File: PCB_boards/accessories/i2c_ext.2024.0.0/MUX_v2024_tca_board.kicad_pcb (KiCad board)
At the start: 2 copper layers, 75 x 50 mm, 18 parts, among them J1 I2C, J2 I2C, J3 I2C, J4 I2C, J5 I2C, J6 I2C, J7 I2C, J8 I2C, J9 I2C

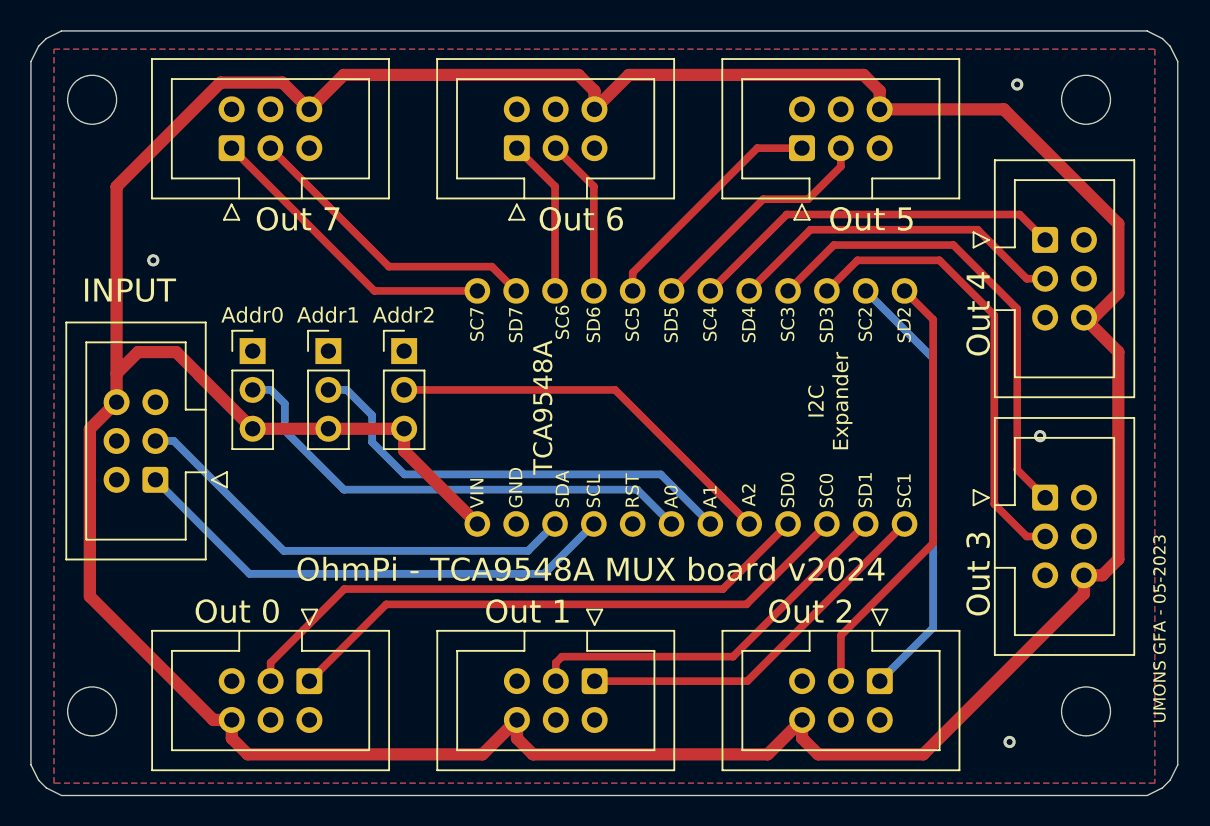
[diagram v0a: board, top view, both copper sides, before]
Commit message: updates I2C_ext board pcb
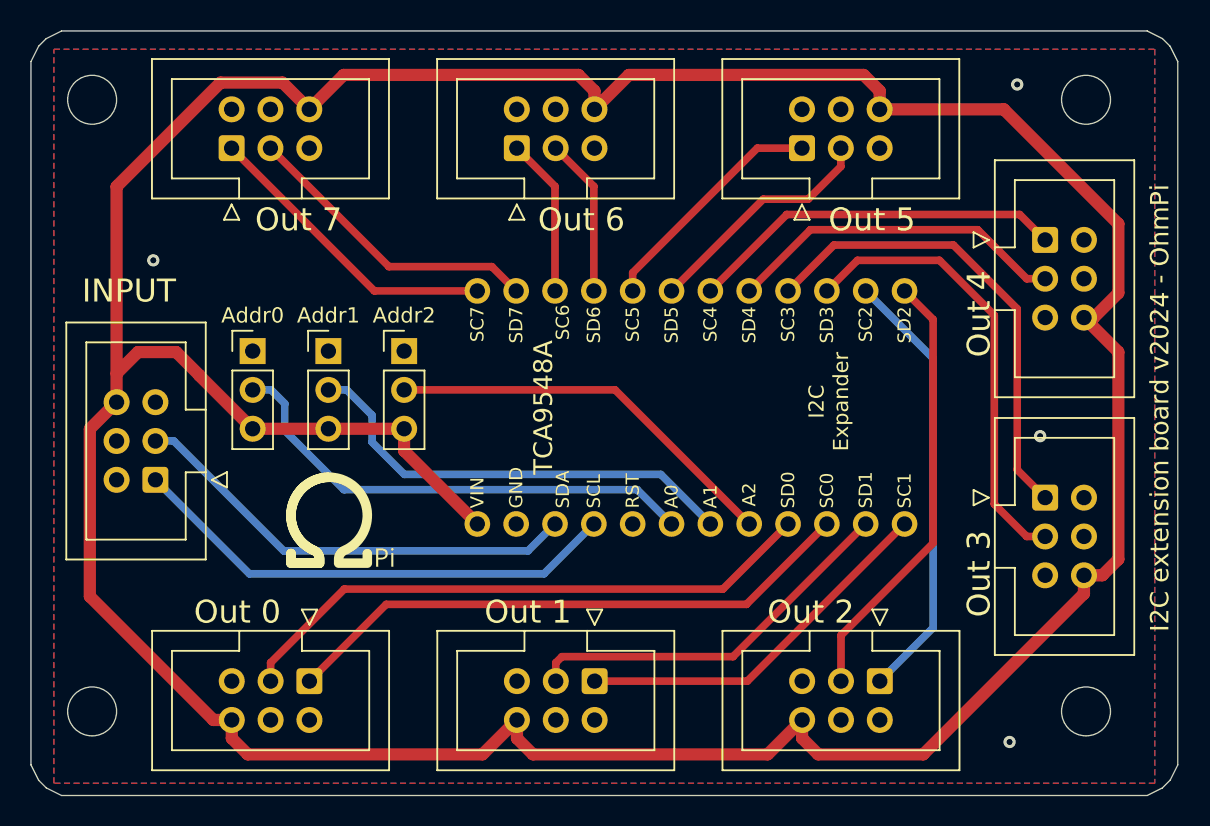
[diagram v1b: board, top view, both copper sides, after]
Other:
- board text added: "I2C extension board v2024 - OhmPi"
- board text removed: "OhmPi - TCA9548A MUX board v2024"
- board text removed: "UMONS GFA - 05-2023"
